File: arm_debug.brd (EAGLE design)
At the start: 28 x 40 mm, 14 parts, among them P1 FTSH-105-01-L-DV-K-TR, P2 FTSH-105-01-L-DV-K-TR, P3 MOLEX_MICRO_USB, P4 MEC6-110-02-L-D-RA1, U1 FT234XD-T

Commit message: Fixing issue with reversed USB Data plus and minus pins
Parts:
- moved R5 3.54 mm to (9.50, 22.5)
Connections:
- net D+: now also U1.12; no longer U1.1
- net D-: now also U1.1; no longer U1.12
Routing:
- net !RESET: track 42.7 -> 39.0 mm
- net TARGET_PWR: track 56.9 -> 53.7 mm
- net D+: track 5.10 -> 7.26 mm
- net D-: track 5.08 -> 7.03 mm, vias 0 -> 2
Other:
- board text added: "github.com/stephendpmurphy"
- board text removed: "github.com/murphtech"
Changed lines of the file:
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@@
 <?xml version="1.0" encoding="utf-8"?>
 <!DOCTYPE eagle SYSTEM "eagle.dtd">
-<eagle version="9.3.2">
+<eagle version="9.5.1">
 <drawing>
 <settings>
-<setting alwaysvectorfont="no"/>
+<setting alwaysvectorfont="yes"/>
 <setting verticaltext="up"/>
 </settings>
@@
 <text x="19.9" y="11.3" size="1.016" layer="25">PROG</text>
 <text x="3.2" y="11.4" size="1.016" layer="25">TARGET</text>
-<text x="7.5" y="24" size="0.8128" layer="25" rot="R90">github.com/murphtech</text>
+<text x="7.5" y="22.5" size="0.8128" layer="25" rot="R90">github.com/stephendpmurphy</text>
 </plain>
 <attributes>
@@
 <attribute name="VALUE" x="17.36375" y="32.545" size="1.27" layer="27" rot="R270"/>
 </element>
-<element name="R5" library="resistor" library_urn="urn:adsk.eagle:library:348" package="R0603" package3d_urn="urn:adsk.eagle:package:26057/1" value="1K" x="6" y="23" smashed="yes" rot="R180">
-<attribute name="NAME" x="4.5" y="22.5" size="0.8128" layer="25" rot="R90"/>
-<attribute name="VALUE" x="6.635" y="24.905" size="1.27" layer="27" rot="R180"/>
+<element name="R5" library="resistor" library_urn="urn:adsk.eagle:library:348" package="R0603" package3d_urn="urn:adsk.eagle:package:26057/1" value="1K" x="9.5" y="22.5" smashed="yes" rot="R180">
+<attribute name="NAME" x="11" y="21.5" size="0.8128" layer="25" rot="R180"/>
+<attribute name="VALUE" x="10.135" y="24.405" size="1.27" layer="27" rot="R180"/>
 </element>
 <element name="P1" library="programming_headers" package="SAMTEC_FTSH-105-01-L-DV-K" value="FTSH-105-01-L-DV-K-TR" x="22" y="17" smashed="yes" rot="R180">
@@
 <attribute name="MF" value="Wurth Electronics" x="14" y="20" size="1.778" layer="27" rot="R90" display="off"/>
 <attribute name="MP" value="431151015826" x="14" y="20" size="1.778" layer="27" rot="R90" display="off"/>
-<attribute name="NAME" x="11.443190625" y="22.46" size="0.8128" layer="25" rot="R90"/>
+<attribute name="NAME" x="17.443190625" y="22.46" size="0.8128" layer="25" rot="R90"/>
 <attribute name="PACKAGE" value="None" x="14" y="20" size="1.778" layer="27" rot="R90" display="off"/>
 <attribute name="PRICE" value="None" x="14" y="20" size="1.778" layer="27" rot="R90" display="off"/>
@@
 <wire x1="19.46" y1="15.76" x2="19.46" y2="14.968" width="0.1524" layer="1"/>
 <wire x1="13.15" y1="16" x2="19.3" y2="16" width="0.1524" layer="1"/>
-<wire x1="13" y1="20" x2="13" y2="18" width="0.1524" layer="1"/>
-<wire x1="6.85" y1="23" x2="10" y2="23" width="0.1524" layer="1"/>
-<wire x1="10" y1="23" x2="13" y2="20" width="0.1524" layer="1"/>
+<wire x1="13" y1="18" x2="13" y2="20" width="0.1524" layer="1"/>
 <wire x1="13" y1="18" x2="12.15" y2="17.15" width="0.1524" layer="1"/>
 <wire x1="12.15" y1="17.15" x2="12.15" y2="17" width="0.1524" layer="1"/>
+<wire x1="13" y1="20" x2="10.5" y2="22.5" width="0.1524" layer="1"/>
+<wire x1="10.5" y1="22.5" x2="10.35" y2="22.5" width="0.1524" layer="1"/>
 </signal>
 <signal name="+5V">
@@
 <contactref element="R1" pad="1"/>
 <contactref element="C1" pad="1"/>
-<contactref element="U1" pad="12"/>
 <wire x1="15.14125" y1="31.06" x2="15.3" y2="31.06" width="0.1524" layer="1"/>
 <wire x1="15.3" y1="31.06" x2="17.205" y2="31.06" width="0.1524" layer="1"/>
-<wire x1="15.48" y1="28.11375" x2="15.48" y2="30.88" width="0.1524" layer="1"/>
 <wire x1="15.48" y1="30.88" x2="15.3" y2="31.06" width="0.1524" layer="1"/>
+<contactref element="U1" pad="1"/>
+<wire x1="15.14125" y1="31.06" x2="15.08125" y2="31" width="0.1524" layer="1"/>
+<wire x1="15.08125" y1="31" x2="14" y2="31" width="0.1524" layer="1"/>
+<via x="14" y="31" extent="1-16" drill="0.35"/>
+<wire x1="14" y1="31" x2="12.5" y2="29.5" width="0.1524" layer="16"/>
+<wire x1="12.5" y1="29.5" x2="12.5" y2="29" width="0.1524" layer="16"/>
+<via x="12.5" y="29" extent="1-16" drill="0.35"/>
+<wire x1="12.5" y1="29" x2="12.58" y2="28.92" width="0.1524" layer="1"/>
+<wire x1="12.58" y1="28.92" x2="12.58" y2="28.11375" width="0.1524" layer="1"/>
 </signal>
 <signal name="D+">
 <contactref element="R7" pad="1"/>
 <contactref element="C2" pad="1"/>
-<contactref element="U1" pad="1"/>
 <wire x1="12.91875" y1="31.06" x2="12.8" y2="31.06" width="0.1524" layer="1"/>
 <wire x1="12.8" y1="31.06" x2="10.855" y2="31.06" width="0.1524" layer="1"/>
-<wire x1="12.58" y1="28.11375" x2="12.58" y2="30.84" width="0.1524" layer="1"/>
 <wire x1="12.58" y1="30.84" x2="12.8" y2="31.06" width="0.1524" layer="1"/>
+<contactref element="U1" pad="12"/>
+<wire x1="12.91875" y1="31.06" x2="12.91875" y2="30.08125" width="0.1524" layer="1"/>
+<wire x1="12.91875" y1="30.08125" x2="13.5" y2="29.5" width="0.1524" layer="1"/>
+<wire x1="13.5" y1="29.5" x2="15" y2="29.5" width="0.1524" layer="1"/>
+<wire x1="15" y1="29.5" x2="15.48" y2="29.02" width="0.1524" layer="1"/>
+<wire x1="15.48" y1="29.02" x2="15.48" y2="28.11375" width="0.1524" layer="1"/>
 </signal>
 <signal name="TARGET_PWR">
@@
 <wire x1="26" y1="19" x2="25.968" y2="19.032" width="0.1524" layer="1"/>
 <wire x1="25.968" y1="19.032" x2="24.54" y2="19.032" width="0.1524" layer="1"/>
-<wire x1="5.15" y1="23" x2="5.15" y2="21.95" width="0.1524" layer="1"/>
-<wire x1="5.6" y1="21.5" x2="8" y2="21.5" width="0.1524" layer="1"/>
-<wire x1="8" y1="21.5" x2="8.6" y2="20.9" width="0.1524" layer="1"/>
-<wire x1="8.6" y1="20.9" x2="8.6" y2="19.092" width="0.1524" layer="1"/>
 <wire x1="8.6" y1="19.092" x2="8.54" y2="19.032" width="0.1524" layer="1"/>
-<wire x1="5.15" y1="21.95" x2="5.6" y2="21.5" width="0.1524" layer="1"/>
 <wire x1="26.9078" y1="18.0922" x2="26" y2="19" width="0.1524" layer="1"/>
 <wire x1="11.1425" y1="1.641" x2="11.6913" y2="1.0922" width="0.1524" layer="1"/>
@@
 <wire x1="11.6913" y1="1.0922" x2="20.0922" y2="1.0922" width="0.1524" layer="1"/>
 <wire x1="26.9078" y1="7.9078" x2="26.9078" y2="18.0922" width="0.1524" layer="1"/>
+<wire x1="8.65" y1="22.5" x2="8.54" y2="22.39" width="0.1524" layer="1"/>
+<wire x1="8.54" y1="22.39" x2="8.54" y2="19.032" width="0.1524" layer="1"/>
 </signal>
 <signal name="N$2">

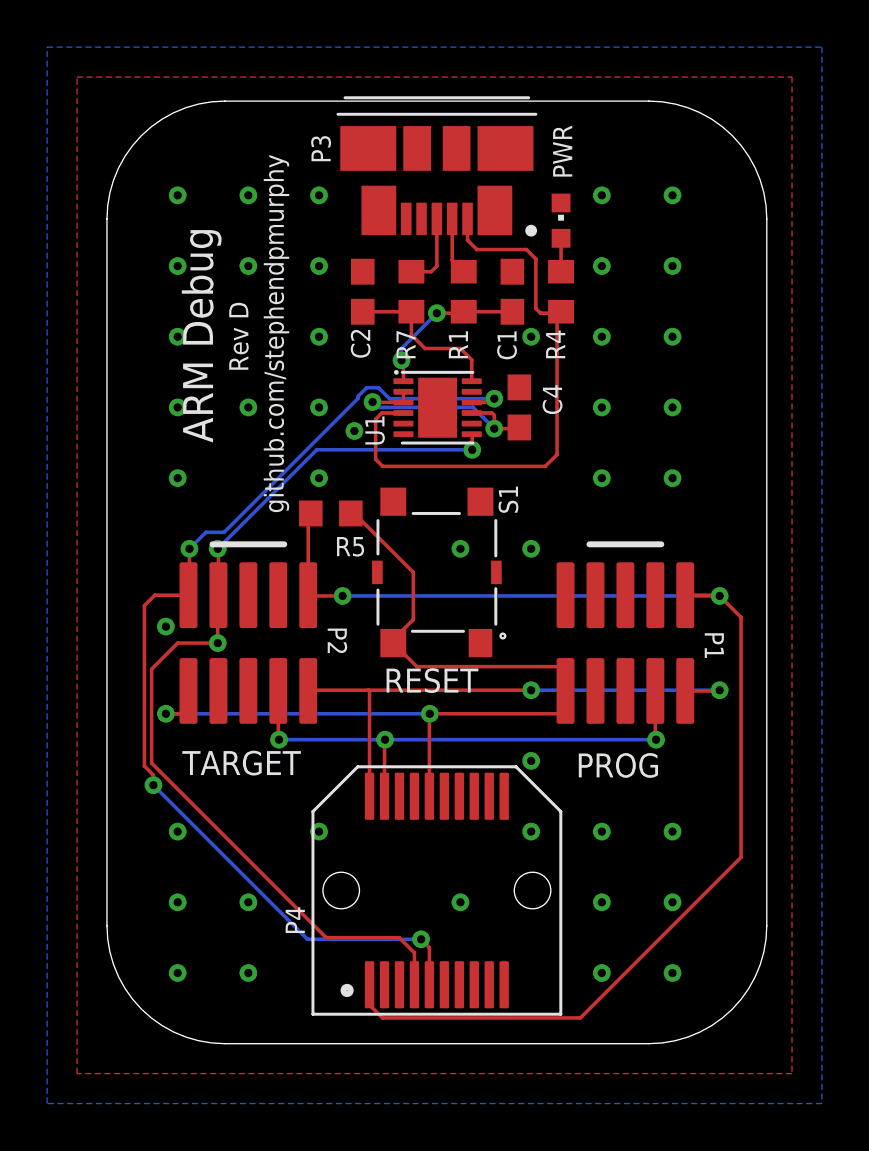
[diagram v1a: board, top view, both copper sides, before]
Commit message: Seperating passive components into individual managed libraries
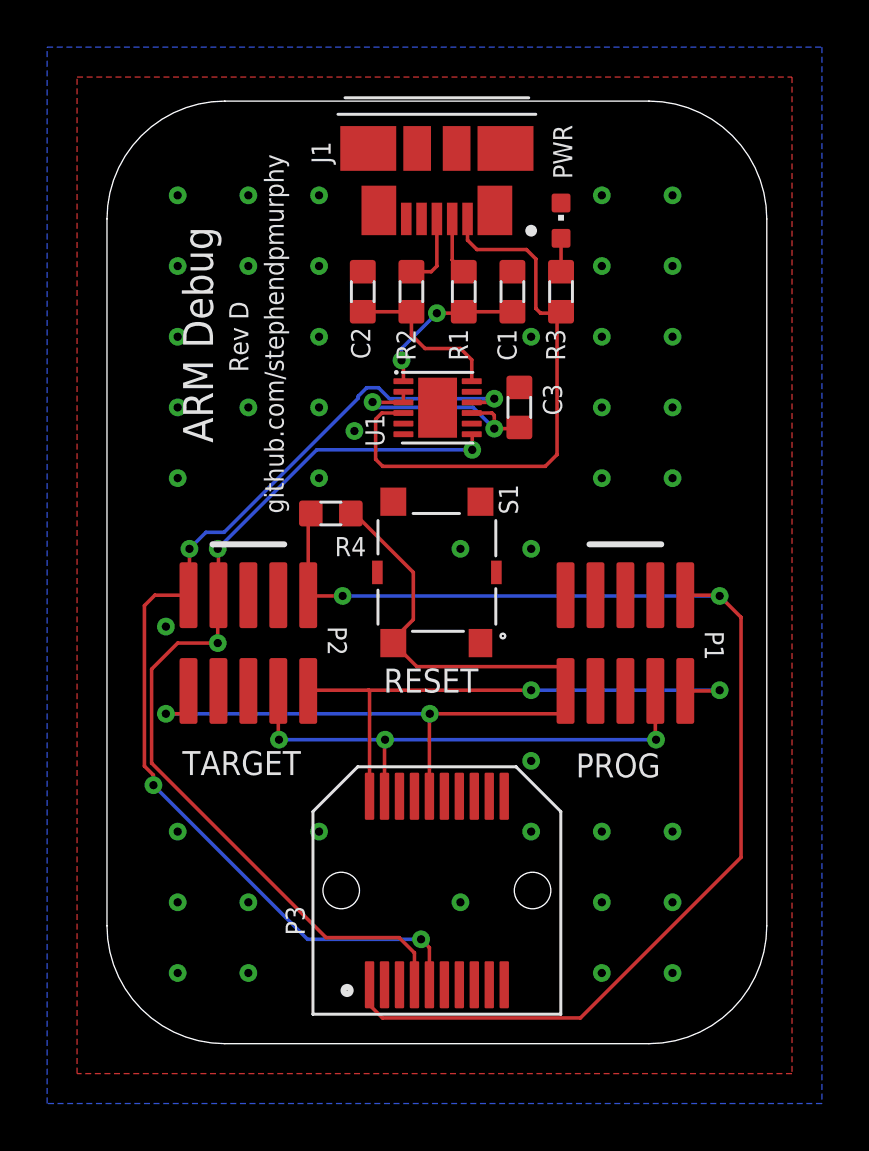
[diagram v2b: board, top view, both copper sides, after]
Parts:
- removed C4: .1uF, resistor:C0603
- removed LED3: (no value), led:CHIPLED_0603
- removed P4: MEC6-110-02-L-D-RA1, programming_headers:MEC6-110-02-X-D-RAX-F
- removed R5: 1K, resistor:R0603
- removed R7: 27, resistor:R0603
- added C3: 0.1uF, capacitors:M0603
- added DS1: (no value), leds:0603
- added J1: 0473460001, board_connectivity:047346-0001
- added R2: 27, resistors:M0603
- added R3: 330, resistors:M0603
- C1, C2: value 47pF -> 22pF; device resistor:C0603 -> capacitors:M0603
- P3: value MOLEX_MICRO_USB -> MEC6-110-02-L-D-RA1; device board_connectivity:047346-0001 -> programming_headers:MEC6-110-02-X-D-RAX-F
- R1: device resistor:R0603 -> resistors:M0603
- R4: value 330 -> 1K; device resistor:R0603 -> resistors:M0603
- S1: value WURTH_SMD_PB -> 431181015816
- moved P3 28.5 mm to (14.0, 6.50), turned to 0 degrees
- moved R4 13.6 mm to (9.50, 22.5), turned to 180 degrees
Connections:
- net !RESET: now also P3.10, R4.1; no longer P4.10, R5.1
- net !RESET#: now also C3.1; no longer C4.1
- net +5V: now also J1.1, R3.2; no longer P3.1, R4.2
- net D+: now also R2.1; no longer R7.1
- net DEBUG_UART_RX: now also P3.7; no longer P4.7
- net DEBUG_UART_TX: now also P3.9; no longer P4.9
- net GND: now also C3.2, DS1.C, J1.5, P3.3; no longer C4.2, LED3.C, P3.P1, P3.P2, P3.P3, P3.P4, P3.P5, P3.P6, P4.3, P4.5
- net N$2: now also J1.2; no longer P3.2
- net N$3: now also DS1.A, R3.1; no longer LED3.A, R4.1
- net N$4: now also J1.3, R2.2; no longer P3.3, R7.2
- net SWDCLK: now also P3.4; no longer P4.4
- net SWDIO: now also P3.2; no longer P4.2
- net TARGET_PWR: now also P3.1, R4.2; no longer P4.1, R5.2
